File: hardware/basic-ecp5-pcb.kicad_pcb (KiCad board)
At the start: 4 copper layers, 100 x 68 mm, 70 parts, among them J1 Conn_01x02, J10 Conn_02x05_Odd_Even, J2 Conn_02x20_Odd_Even, J3 Conn_02x06_Odd_Even, J4 Conn_02x06_Odd_Even, J5 Conn_02x06_Odd_Even, J6 Conn_02x06_Odd_Even, J7 Conn_02x06_Odd_Even, J8 Conn_02x06_Odd_Even, J9 Conn_02x20_Odd_Even, Q1 Q_NMOS_GSD, SW1 SW_Push, SW2 SW_Push, U1 ECP5U_45_CABGA256, U2 IS25LP016D-JBLE, U3 TLV62568DBV, U4 TLV62568DBV, U5 TLV73325PDBV, X1 SiT2001B

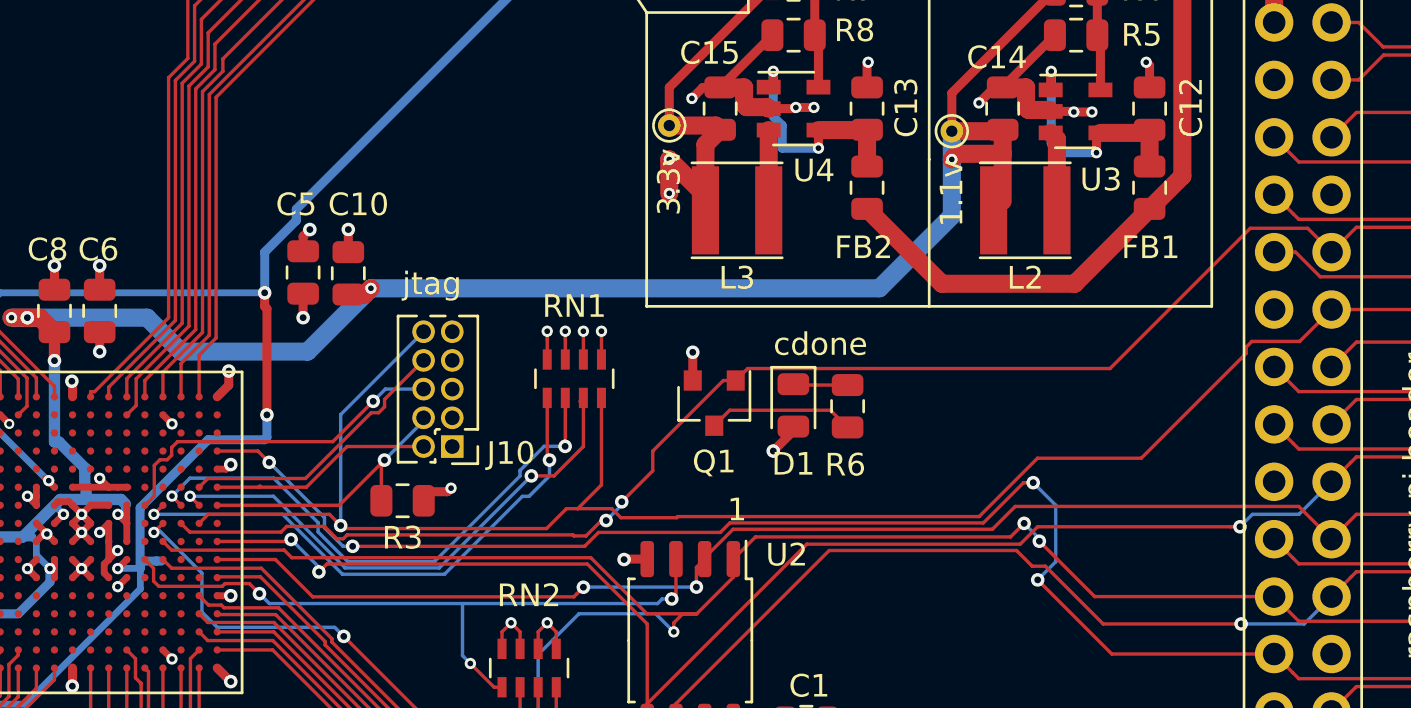
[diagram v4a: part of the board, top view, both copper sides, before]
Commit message: add serial connection
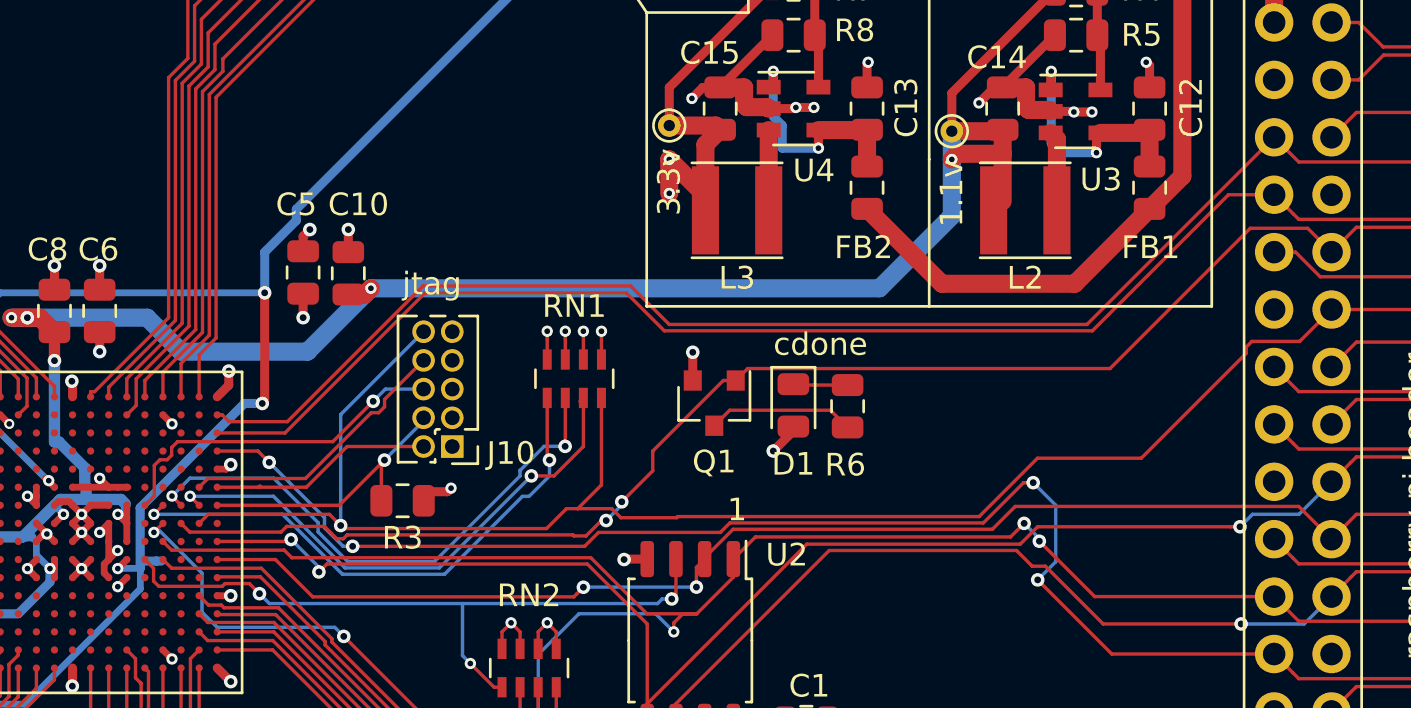
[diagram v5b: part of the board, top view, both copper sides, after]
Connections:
- J2 pad 10: /gp15 -> gp15
- J2 pad 8: /gp14 -> gp14
- J9 pad 10: /gp15 -> gp15
- J9 pad 8: /gp14 -> gp14
- U1 pad T14: Net-(U1-PadT14) -> gp15
- U1 pad T15: Net-(U1-PadT15) -> gp14
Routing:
- net gp14: track 0.00 -> 64.4 mm
- net gp15: track 0.00 -> 63.4 mm
- net /gp15: track 10.9 -> 0.00 mm
- net /gp14: track 10.9 -> 0.00 mm
- net +2V5: track 89.3 -> 88.2 mm

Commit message: ready to order
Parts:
- added 1: TestPoint, TestPoint:TestPoint_THTPad_D1.0mm_Drill0.5mm, F.Cu at (125.8, 85.2)
- added 2: TestPoint, TestPoint:TestPoint_THTPad_D1.0mm_Drill0.5mm, F.Cu at (128.0, 85.2)
- added cf0: TestPoint, TestPoint:TestPoint_THTPad_D1.0mm_Drill0.5mm, F.Cu at (123.5, 85.2)
- J10: footprint Connector_PinHeader_1.27mm:PinHeader_2x05_P1.27mm_Vertical -> Connector_PinHeader_1.27mm:PinHeader_2x05_P1.27mm_Vertical_SMD
- moved J10 2.30 mm to (122.5, 79.9)
- moved RN1 1.00 mm to (128.8, 79.2)
- moved C10 0.10 mm to (117.8, 74.4)
- moved C5 0.10 mm to (115.8, 74.4)
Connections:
- net Net-(RN1-Pad1) renamed /fpga/cfg_0
- net Net-(RN1-Pad2) renamed /fpga/cfg_1
- net Net-(RN1-Pad3) renamed /fpga/cfg_2
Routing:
- net GND: track 75.7 -> 80.3 mm, vias 49 -> 50
- net /fpga/cfg_1: track 24.5 -> 28.9 mm
- net /fpga/cfg_2: track 23.9 -> 26.6 mm
- net /fpga/cfg_0: track 24.5 -> 26.9 mm
- net /fpga/tck: track 12.3 -> 14.3 mm, vias 1 -> 0
- net +3.3VP: track 62.3 -> 64.0 mm, vias 23 -> 24
- net cdone: track 69.0 -> 70.7 mm
- net /fpga/tdo: track 15.4 -> 14.8 mm, vias 1 -> 0
- net /fpga/tms: track 9.96 -> 9.28 mm
- net /fpga/tdi: track 12.4 -> 12.7 mm, vias 0 -> 2
- net creset: track 81.3 -> 81.4 mm, vias 1 -> 2
